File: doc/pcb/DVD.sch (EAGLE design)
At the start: 31 parts, among them IC1 7805, IC2 74HC14N

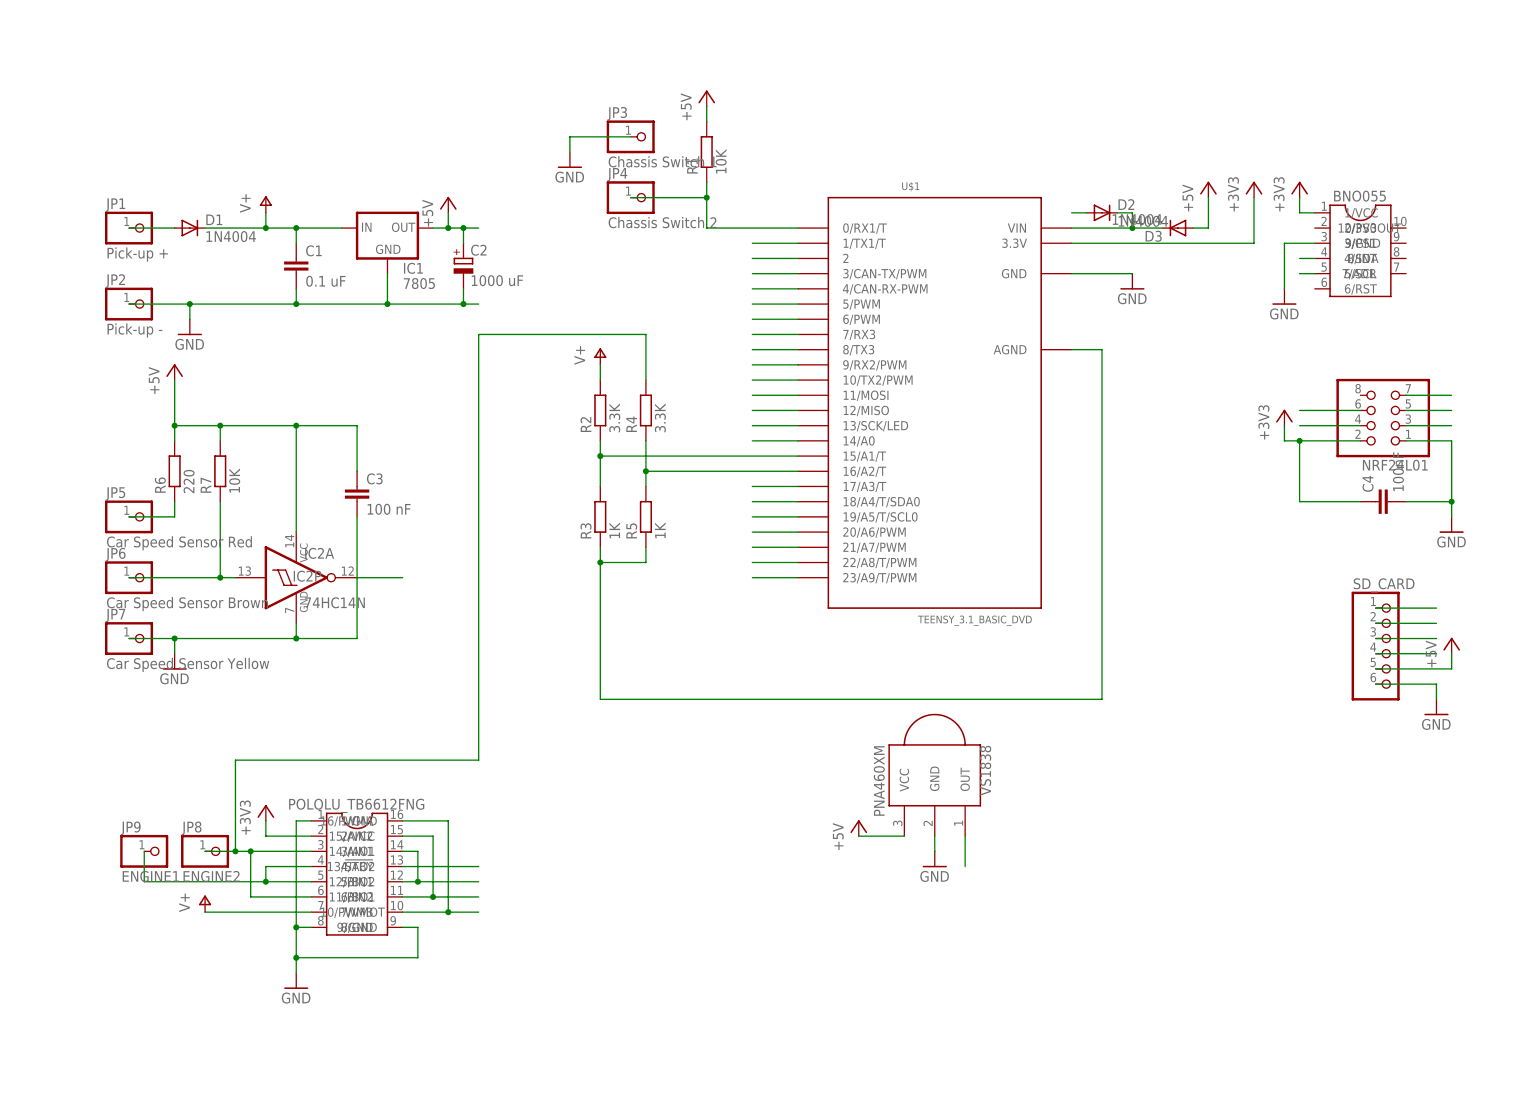
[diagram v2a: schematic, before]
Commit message: Cleanup of Schematics
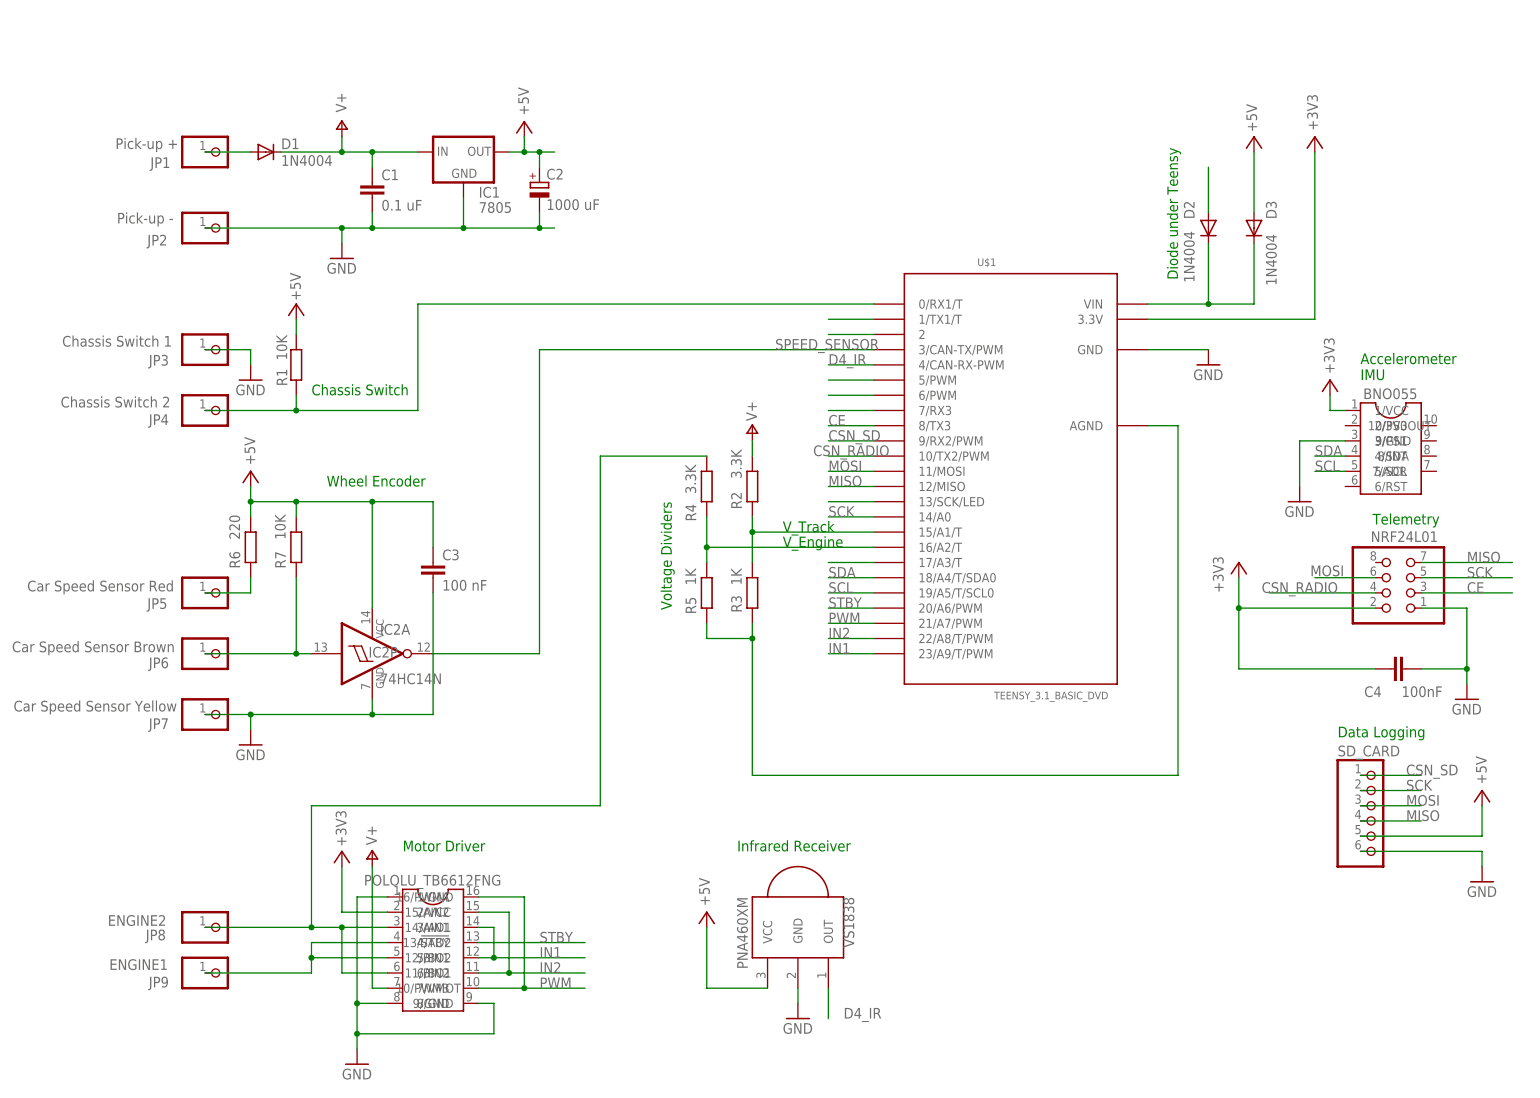
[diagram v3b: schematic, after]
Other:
- note added: "Accelerometer IMU"
- note added: "Chassis Switch"
- note added: "Data Logging"
- note added: "Diode under Teensy"
- note added: "Infrared Receiver"
- note added: "Motor Driver"
- note added: "Telemetry"
- note added: "V_Engine"
- note added: "V_Track"
- note added: "Voltage Dividers"
- note added: "Wheel Encoder"
- moved on the sheet: C1, C2, C3, C4, D1, D2, D3, IC1, IC2A, IC2P, JP1, JP2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

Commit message: Updated schematic and added groundplate to board of PCB
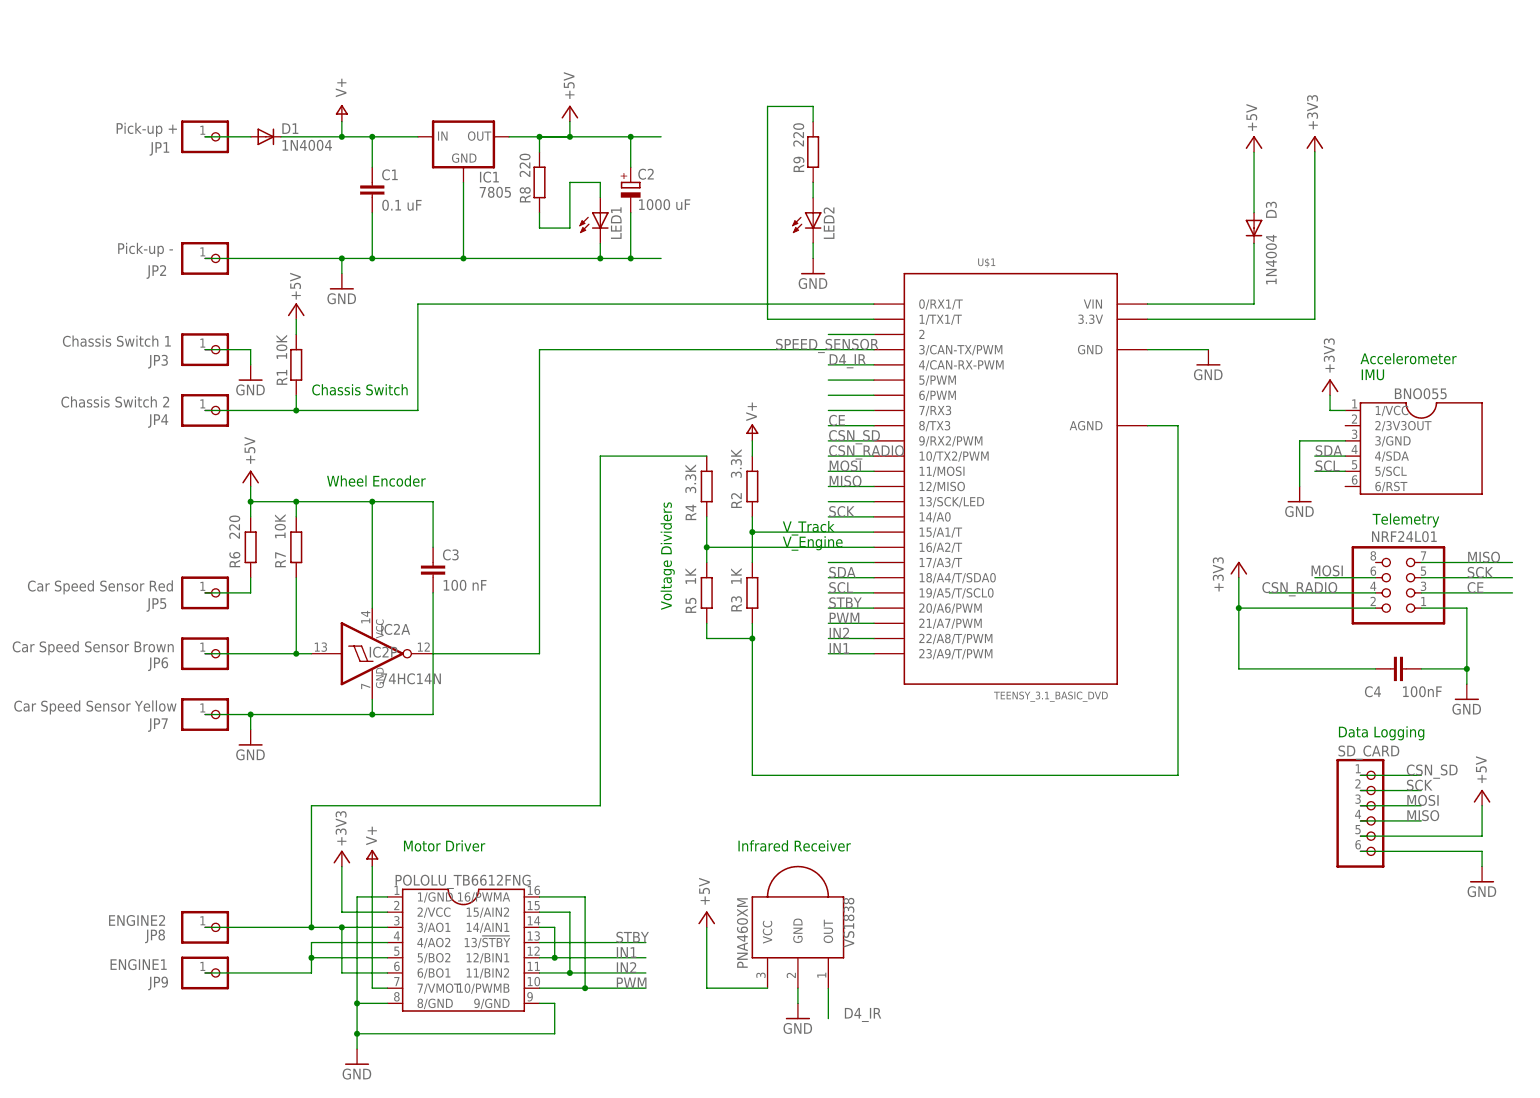
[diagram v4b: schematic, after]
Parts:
- removed D2: 1N4004, adafruit:1N4004
- removed U$4: BNO055, DVD:BNO055
- added LED1, LED2: (no value), adafruit:LED5MM
- added R8, R9: 220, resistor:R-EU_0204/7
- added U$3: BNO055_LIGHT, DVD:BNO055_LIGHT
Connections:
- removed net N$4: D2.A
- new net N$7: LED1.A, R8.1
- new net N$8: LED2.A, R9.1
- net +3V3: now also U$3.1/VCC; no longer U$4.1/VCC
- net +5V: now also R8.2
- net GND: now also LED1.C, LED2.C, U$3.3/GND; no longer U$4.3/GND
- net N$1: no longer D2.C
- net N$19: now also R9.2
- net SCL: now also U$3.5/SCL; no longer U$4.5/SCL
- net SDA: now also U$3.4/SDA; no longer U$4.4/SDA
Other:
- note removed: "Diode under Teensy"
- moved on the sheet: C2, D1, IC1, JP1, JP2

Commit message: LED, caps, beauty
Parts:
- added C5: 100nF, rcl:C-EU025-024X044
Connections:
- removed net N$8: LED2.A, R9.1
- new net N$4: LED2.C, R9.2
- net +5V: now also C1.1, C5.1, LED2.A; no longer C2.+, SD_CARD.5
- net GND: now also C5.2; no longer LED2.C
- net N$19: now also R9.1; no longer R9.2
- net V+: now also C2.+; no longer C1.1
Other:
- note added: "Note: Solder another diode under the Teensy!! (between VUSB and VIN/VREGIN)"
- moved on the sheet: C1, C2, C4, D3, LED1, LED2, NRF24L01, R8, SD_CARD

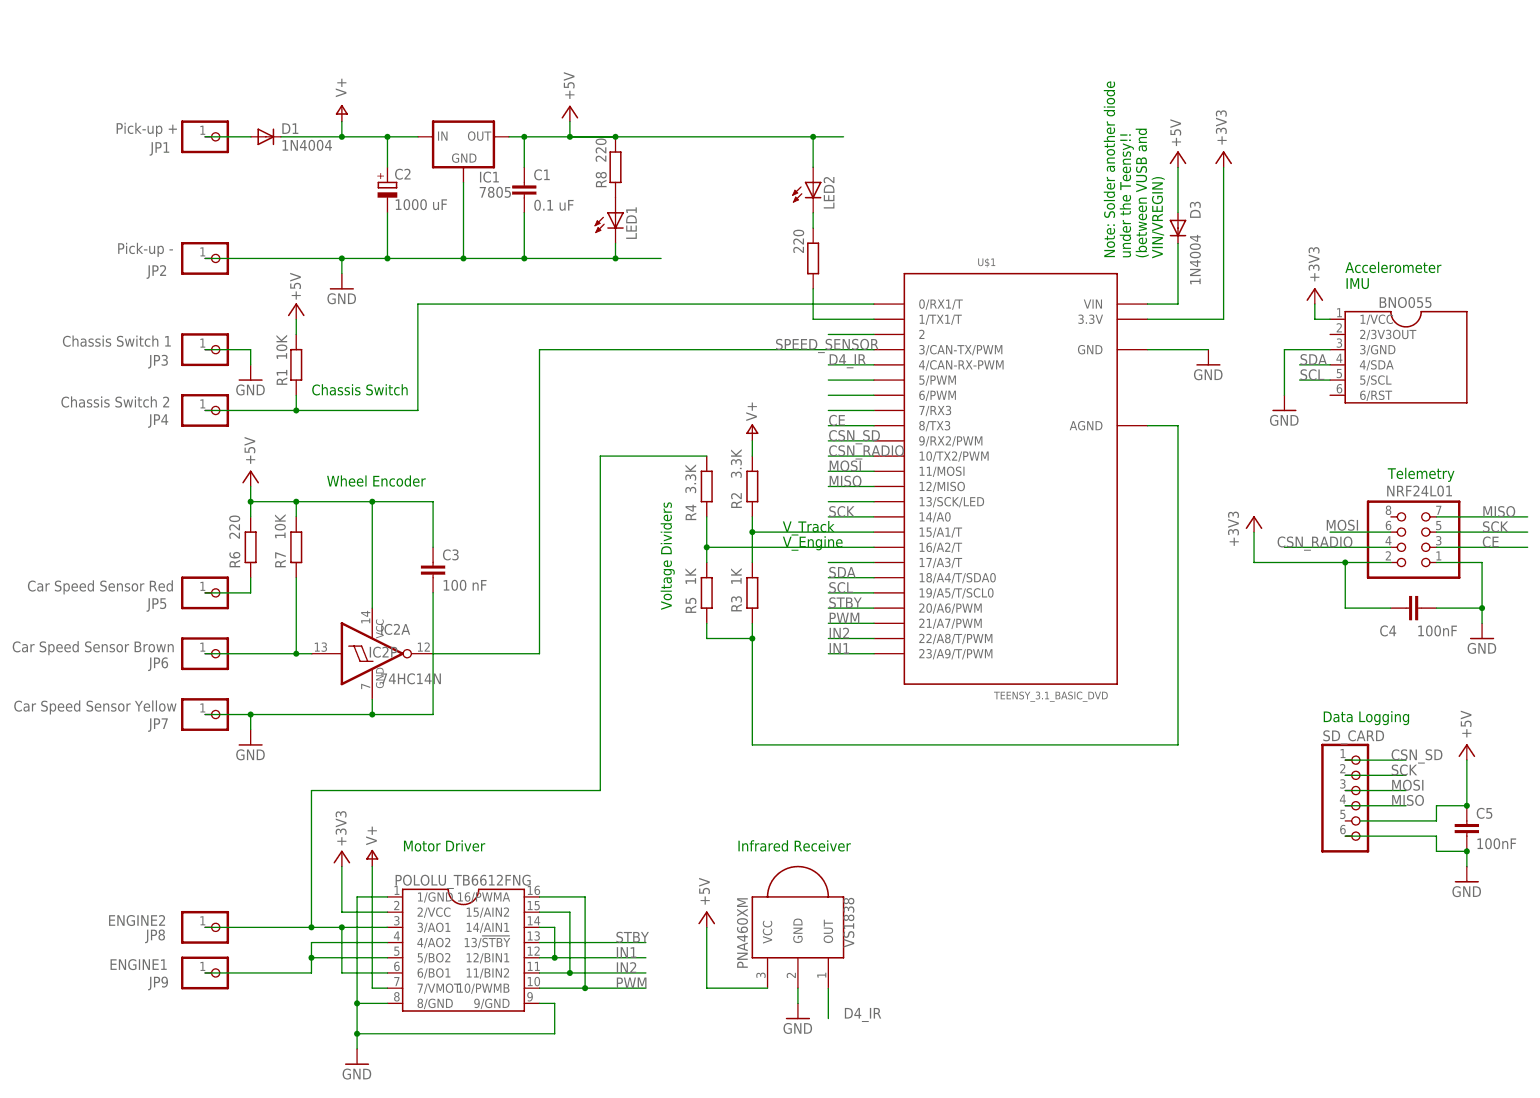
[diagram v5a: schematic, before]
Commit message: PCB moved/added capacitors, changed voltage Pololu/BNO055, added pinouts & testpoints
Only 1 testpoint connected
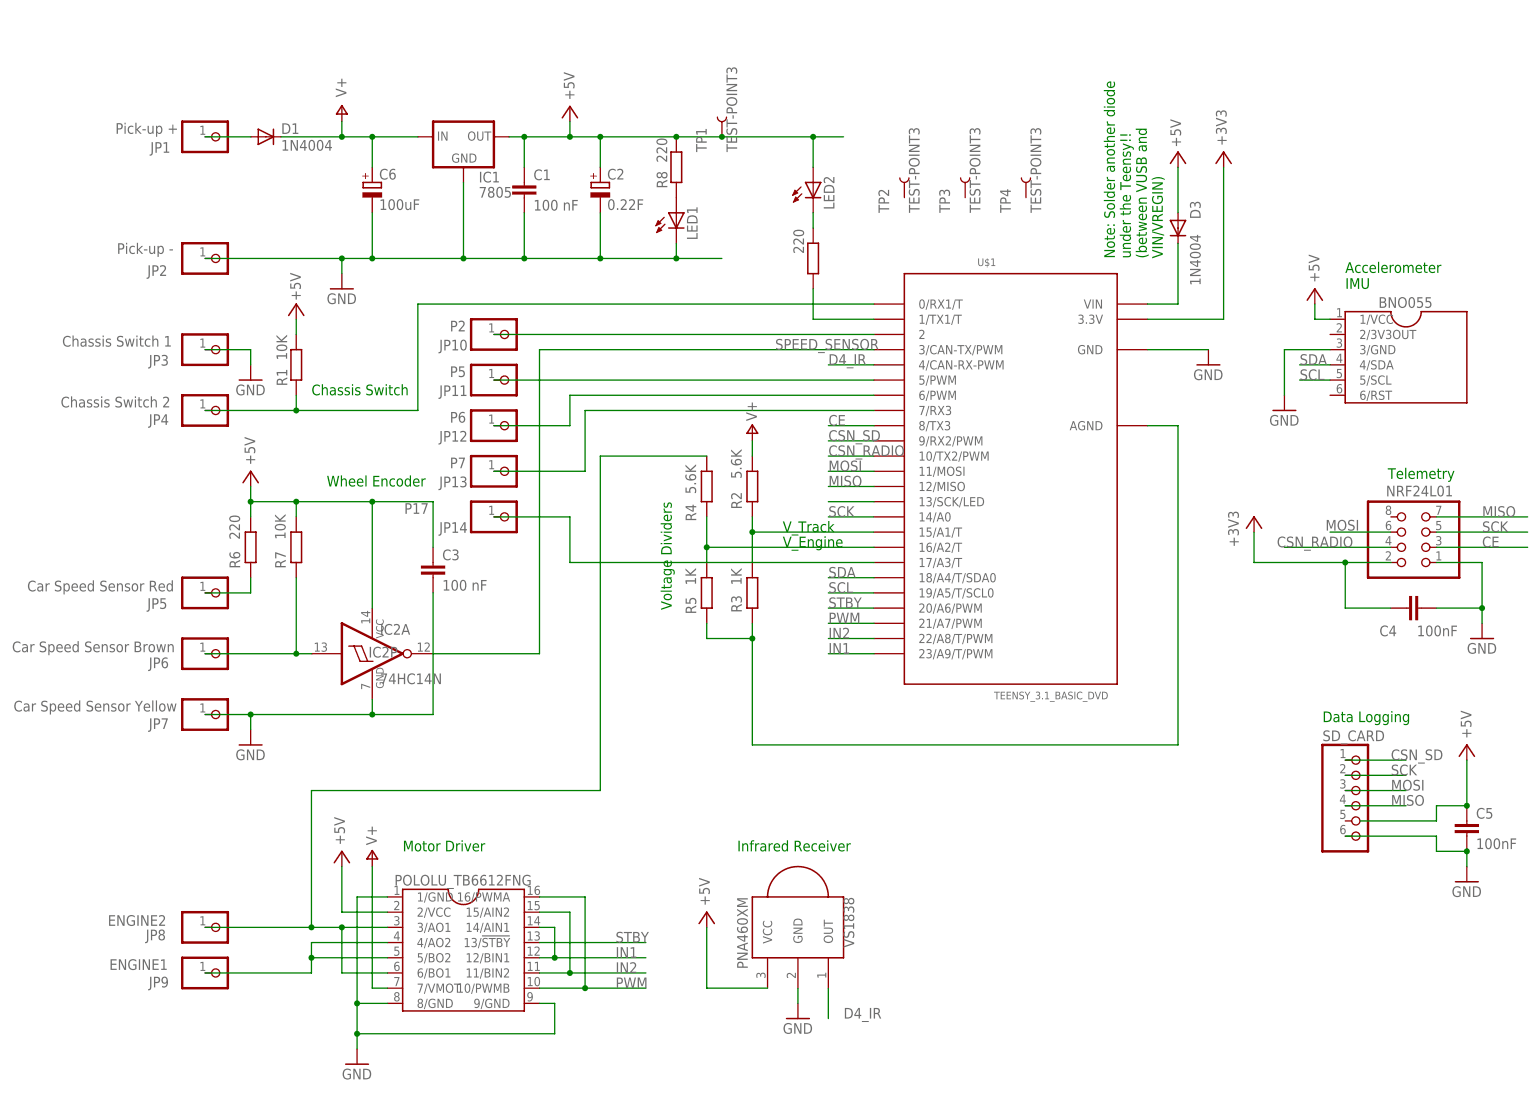
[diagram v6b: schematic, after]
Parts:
- added C6: 100uF, resistor:CPOL-EUE15-6AXIAL
- added JP10: P2, pinhead:PINHD-1X1
- added JP11: P5, pinhead:PINHD-1X1
- added JP12: P6, pinhead:PINHD-1X1
- added JP13: P7, pinhead:PINHD-1X1
- added JP14: P17, pinhead:PINHD-1X1
- added TP1, TP2, TP3, TP4: TEST-POINT3, SparkFun-Passives:TEST-POINT3
- C1: value 0.1 uF -> 100 nF
- C2: value 1000 uF -> 0.22F
- R2, R4: value 3.3K -> 5.6K
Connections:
- net +3V3: no longer U$2.2/VCC, U$3.1/VCC
- net +5V: now also C2.+, TP1.1, U$2.2/VCC, U$3.1/VCC
- net GND: now also C6.-
- net N$20: now also JP10.1
- net N$21: now also JP12.1
- net N$22: now also JP13.1
- net N$3: now also JP11.1
- net N$6: now also JP14.1
- net V+: now also C6.+; no longer C2.+
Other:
- moved on the sheet: C2, LED1, R8
